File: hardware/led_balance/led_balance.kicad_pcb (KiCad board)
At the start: 2 copper layers, 100 x 60 mm, 118 parts, among them J1 Screw_Terminal_01x04, J2 Screw_Terminal_01x02, J3 Screw_Terminal_01x04, J4 Screw_Terminal_01x04, J5 Screw_Terminal_01x04, J6 Screw_Terminal_01x02, J7 Screw_Terminal_01x02, J8 Screw_Terminal_01x02, Q1 Q_NMOS_GDS, Q17 Q_NPN_BEC, Q18 Q_PNP_BEC, Q19 Q_NPN_BEC, Q2 Q_NMOS_GDS, Q20 Q_PNP_BEC, Q21 Q_NPN_BEC, Q22 Q_PNP_BEC, Q23 Q_NPN_BEC, Q24 Q_PNP_BEC, Q25 Q_NPN_BEC, Q26 Q_PNP_BEC, Q27 Q_NPN_BEC, Q28 Q_PNP_BEC, Q29 Q_NPN_BEC, Q3 Q_NMOS_GDS, Q30 Q_PNP_BEC, Q31 Q_NPN_BEC, Q32 Q_PNP_BEC, Q4 Q_NMOS_GDS, Q5 Q_NMOS_GDS, Q6 Q_NMOS_GDS, Q7 Q_NMOS_GDS, Q8 Q_NMOS_GDS

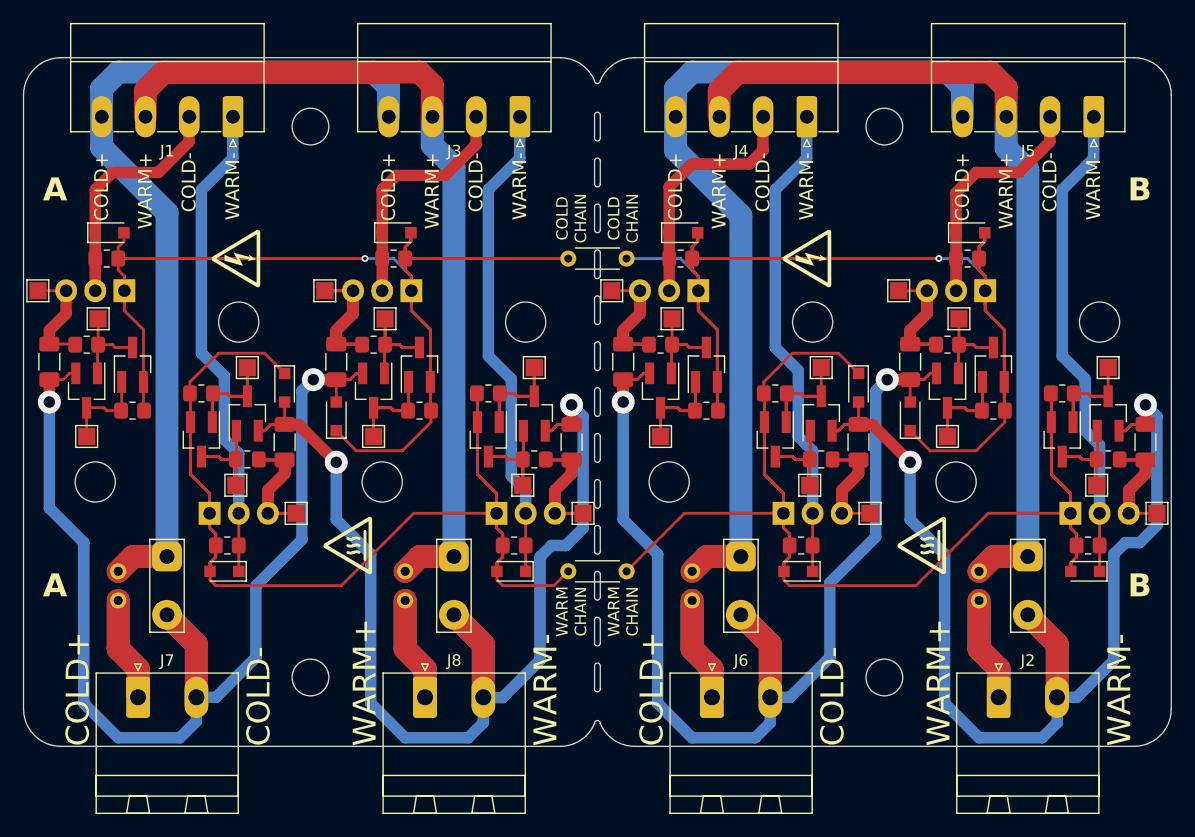
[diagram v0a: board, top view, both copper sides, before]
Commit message: led balance and corridor ready
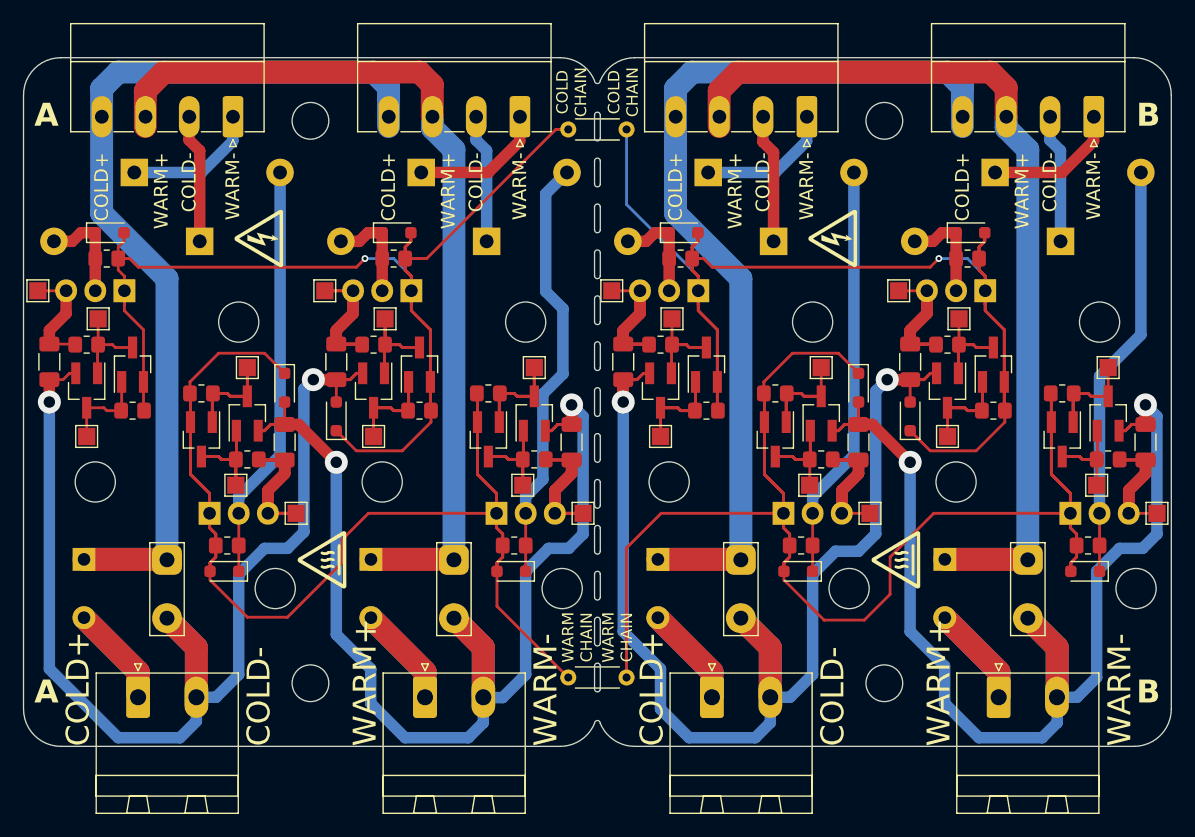
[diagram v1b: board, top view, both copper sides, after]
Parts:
- added D20: 1N5333B, Diode_THT:D_DO-27_P12.70mm_Horizontal, B.Cu at (75.7, 58.5)
- added D21: 1N5333B, Diode_THT:D_DO-27_P12.70mm_Horizontal, B.Cu at (100.7, 58.5)
- added D23: 1N5333B, Diode_THT:D_DO-27_P12.70mm_Horizontal, B.Cu at (125.7, 58.5)
- added D24: 1N5333B, Diode_THT:D_DO-27_P12.70mm_Horizontal, B.Cu at (150.7, 58.5)
- added D25: 1N5333B, Diode_THT:D_DO-27_P12.70mm_Horizontal, B.Cu at (81.3, 64.5)
- added D26: 1N5333B, Diode_THT:D_DO-27_P12.70mm_Horizontal, B.Cu at (106.3, 64.5)
- added D27: 1N5333B, Diode_THT:D_DO-27_P12.70mm_Horizontal, B.Cu at (131.3, 64.5)
- added D28: 1N5333B, Diode_THT:D_DO-27_P12.70mm_Horizontal, B.Cu at (156.3, 64.5)
- TH1, TH2, TH3, TH4: footprint TestPoint:TestPoint_2Pads_Pitch2.54mm_Drill0.8mm -> Package_TO_SOT_THT:TO-220-2_Horizontal_TabUp
- moved R17 11.2 mm to (113.5, 54.8)
- moved R18 9.25 mm to (113.5, 102.5)
- moved TH1 3.16 mm to (71.3, 92.2)
- moved TH2 3.16 mm to (96.3, 92.2)
- moved TH3 3.16 mm to (121.3, 92.2)
- moved TH4 3.16 mm to (146.3, 92.2)
- moved SYM4 2.85 mm to (136.5, 64.2)
- moved SYM2 2.66 mm to (86.5, 64.2)
- moved SYM1 2.57 mm to (92.0, 92.2)
- moved SYM3 2.57 mm to (142.0, 92.2)
- moved H1 0.50 mm to (91.0, 103.0)
- moved H2 0.50 mm to (141.0, 103.0)
- moved H3 0.50 mm to (91.0, 54.0)
- moved H4 0.50 mm to (141.0, 54.0)
- moved TP5 0.29 mm to (78.5, 92.2)
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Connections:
- D1 pad 1: /W0- -> Net-(D1-K)
- D10 pad 1: /W3- -> Net-(D10-K)
- D13 pad 1: /C0- -> Net-(D13-K)
- D16 pad 1: /C1- -> Net-(D16-K)
- D19 pad 1: /C2- -> Net-(D19-K)
- D22 pad 1: /C3- -> Net-(D22-K)
- D4 pad 1: /W1- -> Net-(D21-A)
- D7 pad 1: /W2- -> Net-(D23-A)
- Q1 pad 2: /W0- -> Net-(D1-K)
- Q2 pad 2: /W1- -> Net-(D21-A)
- Q3 pad 2: /W2- -> Net-(D23-A)
- Q4 pad 2: /W3- -> Net-(D10-K)
- Q5 pad 2: /C0- -> Net-(D13-K)
- Q6 pad 2: /C1- -> Net-(D16-K)
- Q7 pad 2: /C2- -> Net-(D19-K)
- Q8 pad 2: /C3- -> Net-(D22-K)
- R1 pad 1: /W0- -> Net-(D1-K)
- R10 pad 1: /W3- -> Net-(D10-K)
- R19 pad 1: /C0- -> Net-(D13-K)
- R22 pad 1: /C1- -> Net-(D16-K)
- R25 pad 1: /C2- -> Net-(D19-K)
- R28 pad 1: /C3- -> Net-(D22-K)
- R4 pad 1: /W1- -> Net-(D21-A)
- R7 pad 1: /W2- -> Net-(D23-A)
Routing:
- net Net-(D21-A): track 0.00 -> 37.5 mm
- net Net-(D23-A): track 0.00 -> 36.2 mm
- net Net-(D10-K): track 0.00 -> 36.2 mm
- net Net-(D1-K): track 0.00 -> 36.2 mm
- net /W3-: track 42.1 -> 11.8 mm
- net /W2-: track 42.1 -> 11.8 mm
- net /W1-: track 42.1 -> 11.8 mm
- net /W0-: track 42.1 -> 11.8 mm
- net /Wb: track 126.8 -> 141.6 mm
- net /C2-: track 21.5 -> 11.2 mm
- net /C1-: track 21.0 -> 11.2 mm
- net /C0-: track 20.9 -> 11.2 mm
- net /C3-: track 20.7 -> 11.2 mm
- net /Cb: track 118.1 -> 127.2 mm
- net Net-(D22-K): track 0.00 -> 8.97 mm
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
